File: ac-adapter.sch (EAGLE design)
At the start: 74 parts, among them IC1 NCP1608, IC2 TL431, Q1 TLP621-1, Q2 600V5A, T1 COMMON_FILTER-SU10VFC, T2 TRANSFORMAER_FLYBACK-PQ2620-2

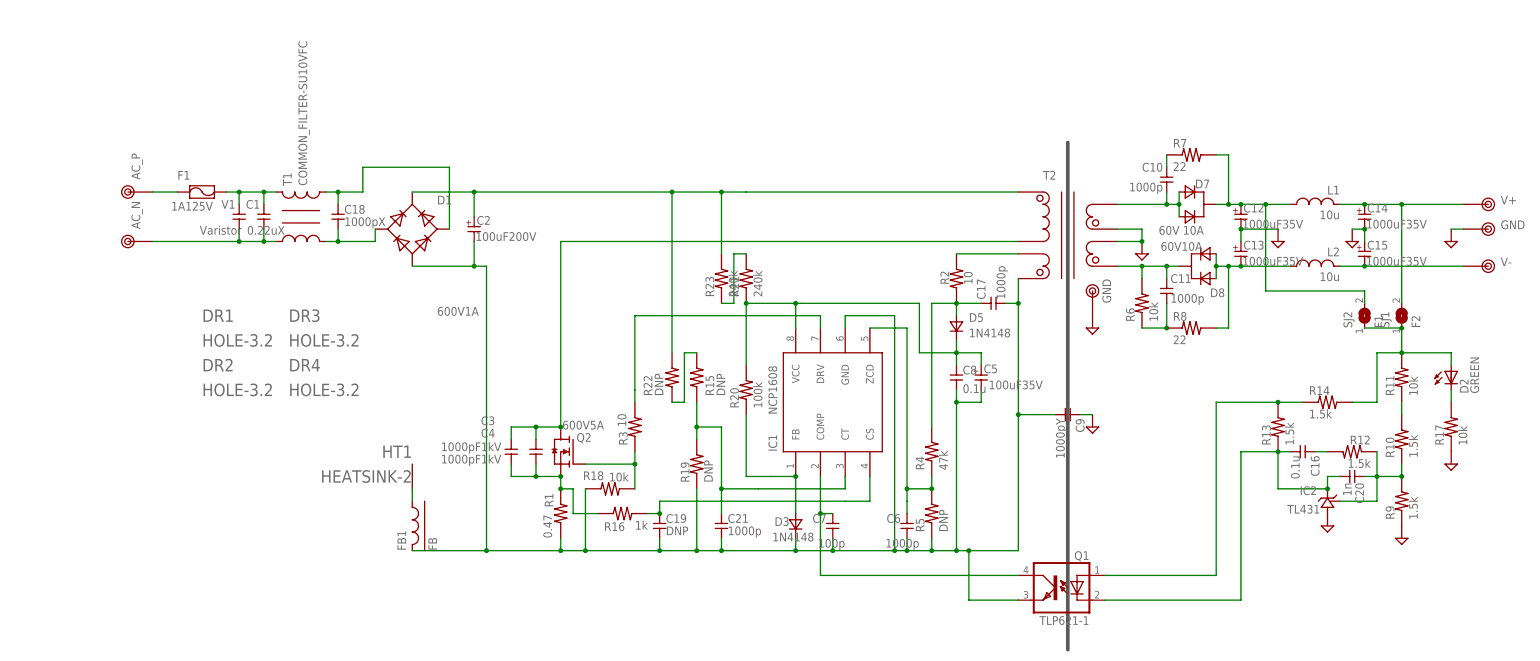
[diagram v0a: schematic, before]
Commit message: GaNに対応
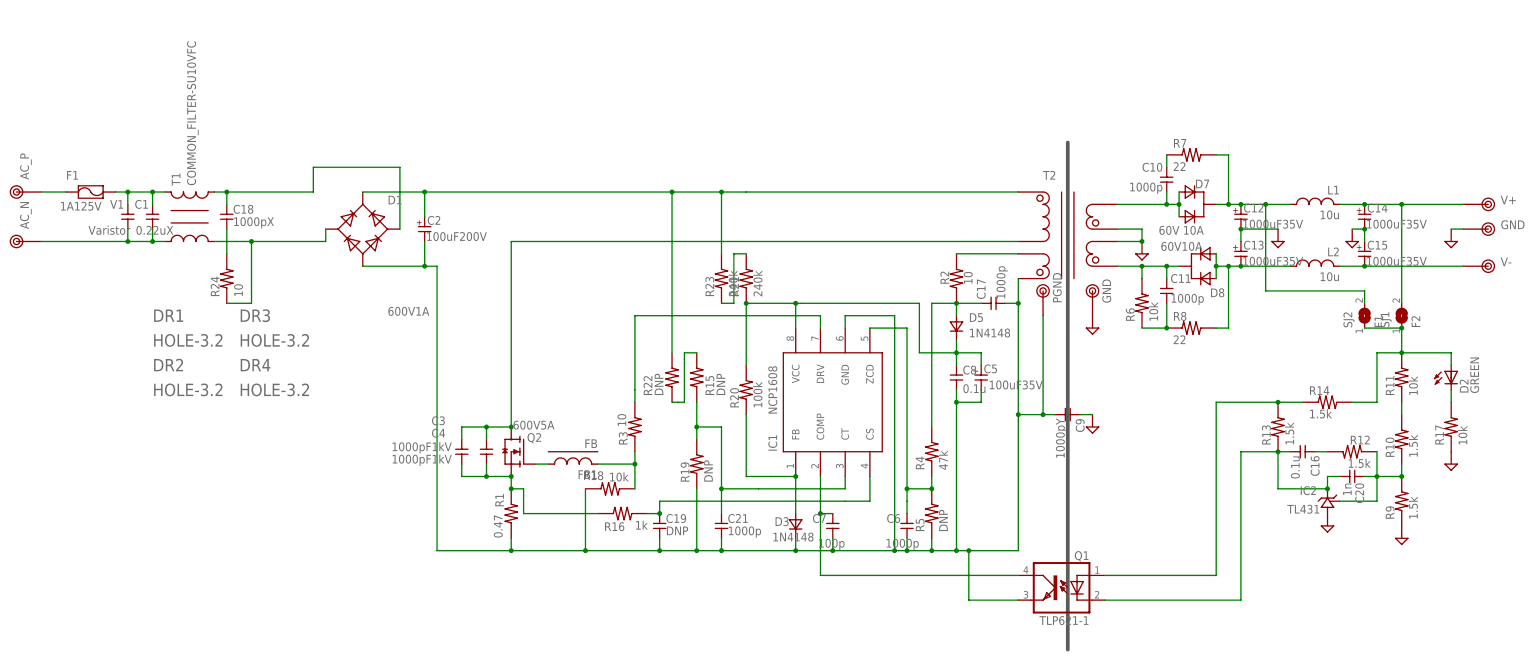
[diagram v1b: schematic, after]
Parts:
- removed HT1: HEATSINK-2, my_connector:HEATSINK-2
- added R24: 10, my_rcl:R-2012
- added TP7: PGND, my_connector:TESTPIN-BIG
- FB1: device my_rcl:FB -> my_rcl:FB-1608FB
- Q2: device my_ic:NMOS -> my_ic:NMOS-GAN
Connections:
- new net N$32: C18.2, R24.2
- net N$14: now also FB1.2; no longer Q2.G
- net N$20: now also Q2.G; no longer HT1.HT
- net N$4: now also R24.1; no longer C18.2
- net PGND: now also TP7.1; no longer FB1.2
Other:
- moved on the sheet: C1, C18, C2, C3, C4, D1, F1, FB1, Q2, R1, T1, V1
